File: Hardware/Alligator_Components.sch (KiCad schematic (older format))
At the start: 113 parts, among them J1 SWD_Header, J2 Eurorack_10_pin_power, J3 Conn_01x08_Female, J4 Conn_01x08_Female, J5 Conn_01x08_Female, J6 Conn_01x08_Female, SW1 SW_SPST, SW2 SW_SPDT_MSM, U1 STM32H743ZITx, U2 IS42S16400J-xC, U3 PCM5100APW, U4 SSI2164, U5 MCP6004, U6 MCP6004, U7 TL074, U8 LM1117-3.3, Y1 8MHz 20pF

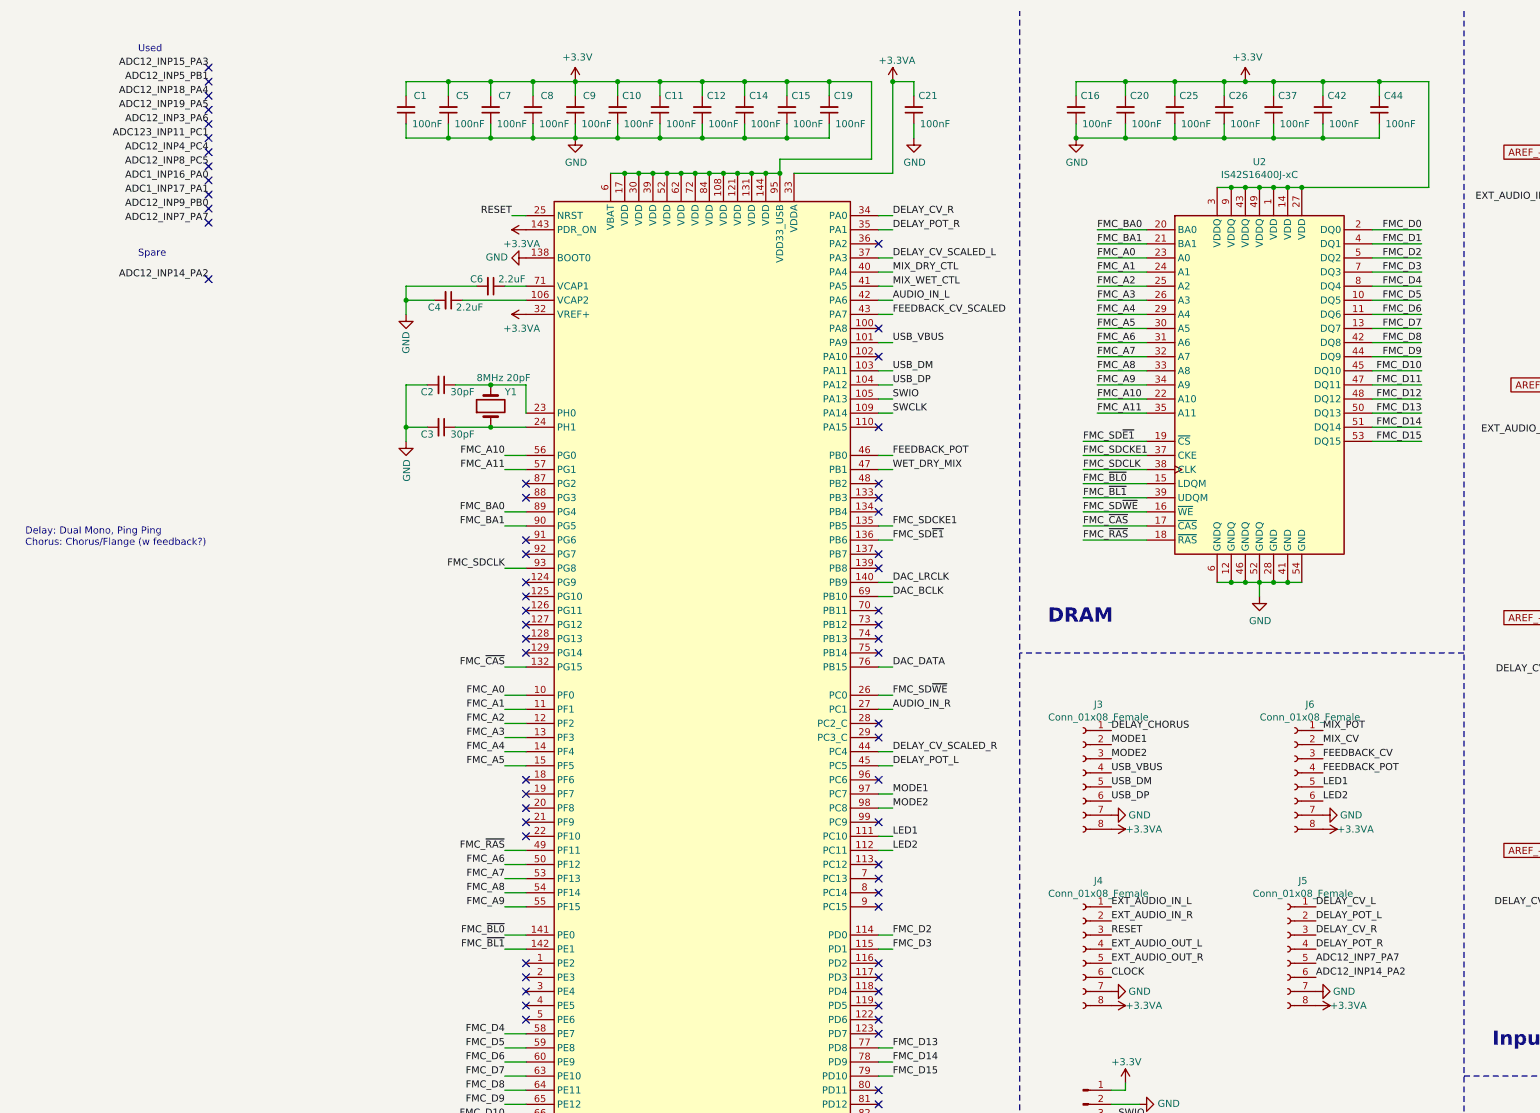
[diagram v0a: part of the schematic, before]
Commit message: Further routing of PCB
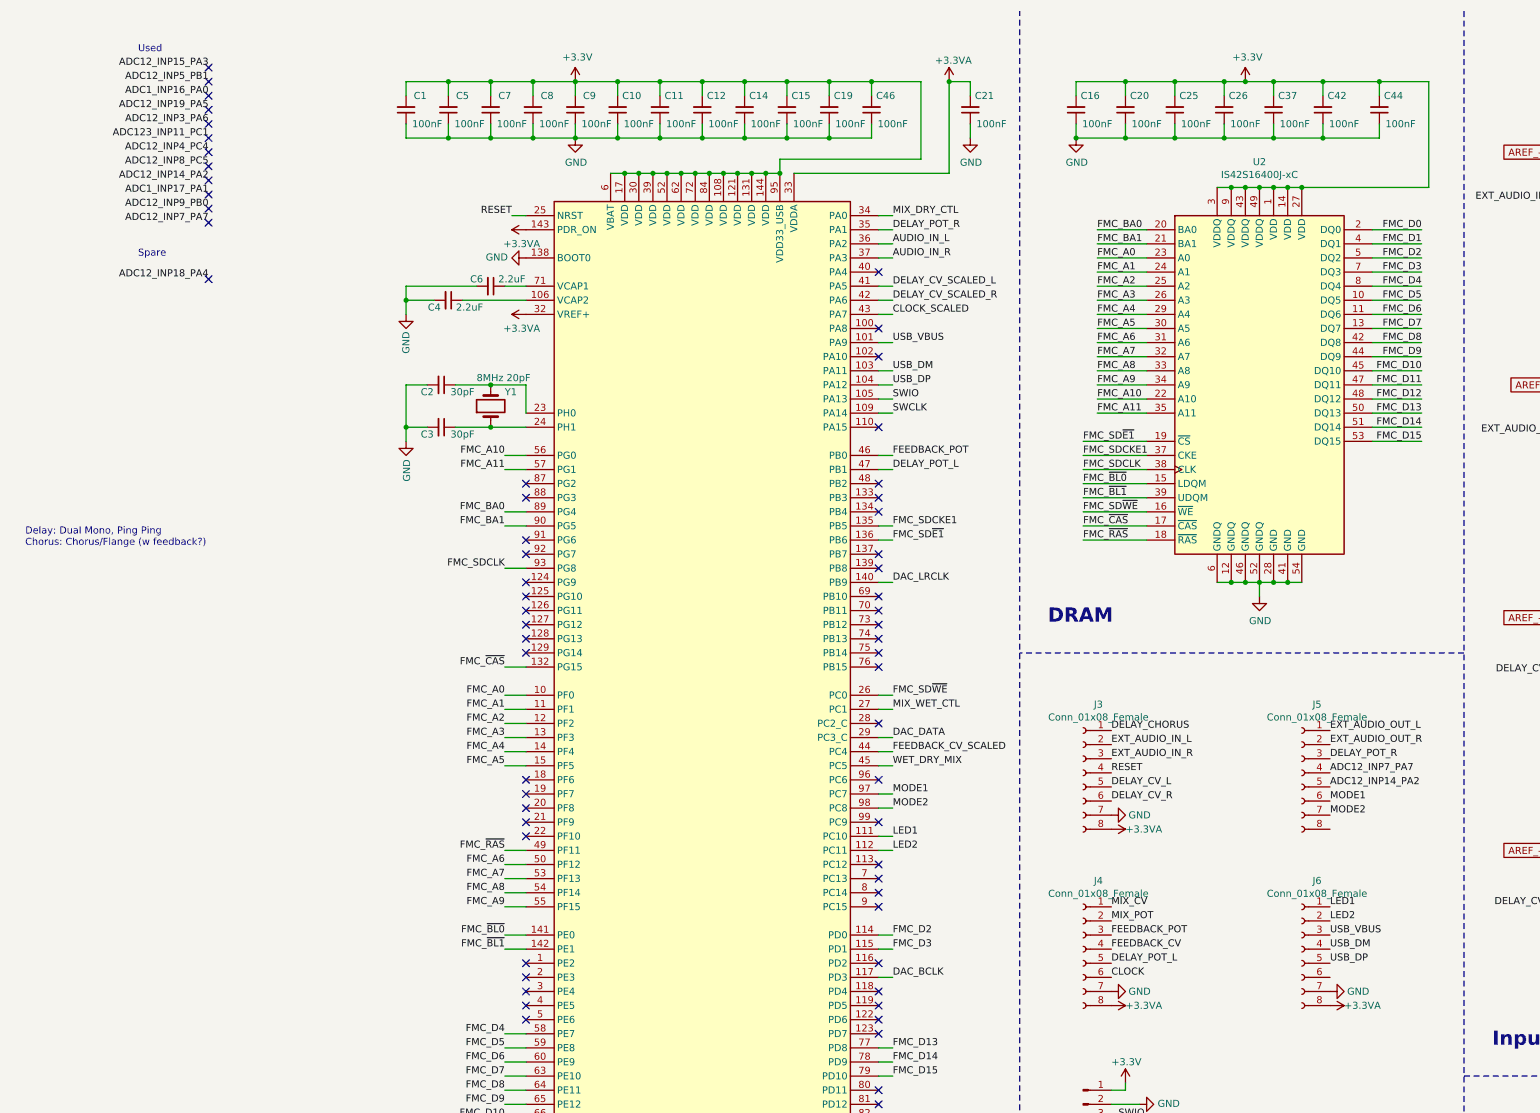
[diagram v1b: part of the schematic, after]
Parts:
- added C46: 100nF, Capacitors_SMD:C_0603_HandSoldering, symbol Device:C_Small
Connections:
- net +3.3VA: no longer J5.8 (Pin_8)
- net +3V3: now also C46.2
- net ADC12_INP14_PA2: now also J5.5 (Pin_5); no longer J5.6 (Pin_6)
- net ADC12_INP7_PA7: now also J5.4 (Pin_4); no longer J5.5 (Pin_5)
- net AUDIO_IN_L: now also U1.36 (PA2); no longer U1.42 (PA6)
- net AUDIO_IN_R: now also U1.37 (PA3); no longer U1.27 (PC1)
- net CLOCK_SCALED: now also U1.43 (PA7)
- net DAC_BCLK: now also U1.117 (PD3); no longer U1.69 (PB10)
- net DAC_DATA: now also U1.29 (PC3_C); no longer U1.76 (PB15)
- net DELAY_CV_L: now also J3.5 (Pin_5); no longer J5.1 (Pin_1)
- net DELAY_CV_R: now also J3.6 (Pin_6); no longer J5.3 (Pin_3), U1.34 (PA0)
- net DELAY_CV_SCALED_L: now also U1.41 (PA5); no longer U1.37 (PA3)
- net DELAY_CV_SCALED_R: now also U1.42 (PA6); no longer U1.44 (PC4)
- net DELAY_POT_L: now also J4.5 (Pin_5), U1.47 (PB1); no longer J5.2 (Pin_2), U1.45 (PC5)
- net DELAY_POT_R: now also J5.3 (Pin_3); no longer J5.4 (Pin_4)
- net EXT_AUDIO_IN_L: now also J3.2 (Pin_2); no longer J4.1 (Pin_1)
- net EXT_AUDIO_IN_R: now also J3.3 (Pin_3); no longer J4.2 (Pin_2)
- net EXT_AUDIO_OUT_L: now also J5.1 (Pin_1); no longer J4.4 (Pin_4)
- net EXT_AUDIO_OUT_R: now also J5.2 (Pin_2); no longer J4.5 (Pin_5)
- net FEEDBACK_CV: now also J4.4 (Pin_4); no longer J6.3 (Pin_3)
- net FEEDBACK_CV_SCALED: now also U1.44 (PC4); no longer U1.43 (PA7)
- net FEEDBACK_POT: now also J4.3 (Pin_3); no longer J6.4 (Pin_4)
- net GND: now also C46.1; no longer J5.7 (Pin_7)
- net LED1: now also J6.1 (Pin_1); no longer J6.5 (Pin_5)
- net LED2: now also J6.2 (Pin_2); no longer J6.6 (Pin_6)
- net MIX_CV: now also J4.1 (Pin_1); no longer J6.2 (Pin_2)
- net MIX_DRY_CTL: now also U1.34 (PA0); no longer U1.40 (PA4)
- net MIX_POT: now also J4.2 (Pin_2); no longer J6.1 (Pin_1)
- net MIX_WET_CTL: now also U1.27 (PC1); no longer U1.41 (PA5)
- net MODE1: now also J5.6 (Pin_6); no longer J3.2 (Pin_2)
- net MODE2: now also J5.7 (Pin_7); no longer J3.3 (Pin_3)
- net RESET: now also J3.4 (Pin_4); no longer J4.3 (Pin_3)
- net USB_DM: now also J6.4 (Pin_4); no longer J3.5 (Pin_5)
- net USB_DP: now also J6.5 (Pin_5); no longer J3.6 (Pin_6)
- net USB_VBUS: now also J6.3 (Pin_3); no longer J3.4 (Pin_4)
- net WET_DRY_MIX: now also U1.45 (PC5); no longer U1.47 (PB1)
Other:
- moved on the sheet: C21, J5, J6

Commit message: Continued routing and reorganising PCB
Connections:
- net +3.3VA: now also J5.2 (Pin_2)
- net +3V3: no longer U1.6 (VBAT)
- net ADC12_INP14_PA2: no longer J5.5 (Pin_5)
- net ADC12_INP7_PA7: no longer J5.4 (Pin_4)
- net DAC_OUT_AMP_L: now also R14.2; no longer R10.2
- net DAC_OUT_AMP_R: now also R10.2; no longer R14.2
- net DELAY_CHORUS: now also J6.6 (Pin_6), U1.119 (PD5); no longer J3.1 (Pin_1)
- net DELAY_POT_R: now also J5.6 (Pin_6); no longer J5.3 (Pin_3)
- net DRY_OUT_L: now also U4.5 (I_OUT2); no longer U4.4 (I_OUT1)
- net DRY_OUT_R: now also U4.4 (I_OUT1); no longer U4.5 (I_OUT2)
- net EXT_AUDIO_OUT_L: now also J5.5 (Pin_5); no longer J5.1 (Pin_1)
- net EXT_AUDIO_OUT_R: now also J5.4 (Pin_4); no longer J5.2 (Pin_2)
- net GND: now also J5.1 (Pin_1)
- net MODE1: now also J5.7 (Pin_7); no longer J5.6 (Pin_6)
- net MODE2: now also J5.8 (Pin_8); no longer J5.7 (Pin_7)
- net at C2.1, Y1.2: no longer U1.23 (PH0)
- no-connect marks 68 -> 67
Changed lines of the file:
@@
 	1500 3450 1750 3450
-Wire Wire Line
-	1750 3350 1750 3150
 Wire Wire Line
 	1750 3150 1500 3150
@@
 Text Label 4350 8050 0    50   ~ 0
 FMC_D15
-Wire Wire Line
-	2450 1650 2550 1650
 Wire Wire Line
 	2550 8850 2650 8850
@@
 Wire Wire Line
 	4350 3750 4250 3750
-Wire Wire Line
-	2350 1650 2450 1650
-Connection ~ 2450 1650
 NoConn ~ 1750 3850
 NoConn ~ 1750 3950
@@
 NoConn ~ 4250 7250
 NoConn ~ 4250 7450
-NoConn ~ 4250 7550
 NoConn ~ 4250 7650
 NoConn ~ 4250 7750
@@
 Text Label 5900 5700 0    50   ~ 0
 EXT_AUDIO_IN_L
-Text Label 7450 5700 0    50   ~ 0
+Text Label 7450 5900 0    50   ~ 0
 EXT_AUDIO_OUT_R
-Text Label 7450 5600 0    50   ~ 0
+Text Label 7450 6000 0    50   ~ 0
 EXT_AUDIO_OUT_L
 Text Label 16450 6800 0    50   ~ 0
@@
 Text Label 16450 5200 0    50   ~ 0
 EXT_AUDIO_OUT_L
+Text Label 15900 9150 0    50   ~ 0
+WET_OUT_L
 Text Label 15900 8850 0    50   ~ 0
-WET_OUT_L
-Text Label 15900 9150 0    50   ~ 0
 WET_OUT_R
 Text Label 15900 9450 0    50   ~ 0
@@
 	-1   0    0    1
 $EndComp
-Text Label 14050 8850 2    50   ~ 0
+Text Label 14050 9150 2    50   ~ 0
 DAC_OUT_AMP_L
 Wire Wire Line
@@
 Wire Wire Line
 	14750 9550 14750 9600
-Text Label 14050 9150 2    50   ~ 0
+Text Label 14050 8850 2    50   ~ 0
 DAC_OUT_AMP_R
 Wire Wire Line
@@
 Text Label 5900 7250 0    50   ~ 0
 DELAY_POT_L
-Text Label 7450 5800 0    50   ~ 0
+Text Label 7450 6100 0    50   ~ 0
 DELAY_POT_R
 Text Label 5900 7050 0    50   ~ 0
@@
 Wire Wire Line
 	14900 1750 14950 1750
-Text Label 5900 5600 0    50   ~ 0
+Text Label 7450 7350 0    50   ~ 0
 DELAY_CHORUS
 Text Notes -1800 4300 0    50   ~ 0
 Delay: Dual Mono, Ping Ping\nChorus: Chorus/Flange (w feedback?)
-Text Label 7450 6100 0    50   ~ 0
+Text Label 7450 6200 0    50   ~ 0
 MODE1
-Text Label 7450 6200 0    50   ~ 0
+Text Label 7450 6300 0    50   ~ 0
 MODE2
 $Comp
@@
 	0    1    1    0
 $EndComp
-Text Label 7450 6000 0    50   ~ 0
-ADC12_INP14_PA2
-Text Label 7450 5900 0    50   ~ 0
-ADC12_INP7_PA7
 $Comp
 L power:GNDA #PWR016
@@
 Wire Wire Line
 	4550 1000 4200 1000
-Connection ~ 3550 1650
 Connection ~ 3900 1000
 Wire Wire Line
@@
 Text Label 7450 6950 0    50   ~ 0
 LED2
+$Comp
+L power:GND #PWR0113
+U 1 1 60A8280D
+P 7450 5600
+F 0 "#PWR0113" H 7450 5350 50  0001 C CNN
+F 1 "GND" V 7450 5400 50  0000 C CNN
+F 2 "" H 7450 5600 50  0001 C CNN
+F 3 "" H 7450 5600 50  0001 C CNN
+	1    7450 5600
+	0    -1   -1   0
+$EndComp
+$Comp
+L power:+3.3VA #PWR0124
+U 1 1 60A82817
+P 7450 5700
+F 0 "#PWR0124" H 7450 5550 50  0001 C CNN
+F 1 "+3.3VA" V 7450 5800 50  0000 L CNN
+F 2 "" H 7450 5700 50  0001 C CNN
+F 3 "" H 7450 5700 50  0001 C CNN
+	1    7450 5700
+	0    1    1    0
+$EndComp
+Text Label 4350 7550 0    50   ~ 0
+DELAY_CHORUS
+Wire Wire Line
+	1750 3250 1750 3150
+Wire Wire Line
+	2450 1650 2550 1650
+Connection ~ 3550 1650
+Wire Wire Line
+	4250 7550 4350 7550
 $EndSCHEMATC

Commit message: Further updates to pcb layout
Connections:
- net +3V3: now also U1.6 (VBAT)
- net DELAY_CHORUS: now also J6.1 (Pin_1), U1.113 (PC12); no longer J6.6 (Pin_6), U1.119 (PD5)
- net DELAY_CV_SCALED_L: now also U1.34 (PA0); no longer U1.41 (PA5)
- net LED1: now also J6.3 (Pin_3); no longer J6.1 (Pin_1)
- net MIX_DRY_CTL: now also U1.40 (PA4); no longer U1.34 (PA0)
- net MIX_WET_CTL: now also U1.41 (PA5); no longer U1.27 (PC1)
- net MODE1: now also U1.1 (PE2); no longer U1.97 (PC7)
- net MODE2: now also U1.2 (PE3); no longer U1.98 (PC8)
- net USB_DM: now also J6.5 (Pin_5); no longer J6.4 (Pin_4)
- net USB_DP: now also J6.4 (Pin_4); no longer J6.5 (Pin_5)
- net USB_VBUS: now also J6.6 (Pin_6); no longer J6.3 (Pin_3)
- net at C2.1, Y1.2: now also U1.23 (PH0)
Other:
- moved on the sheet: J1, J3, J4, J5, J6

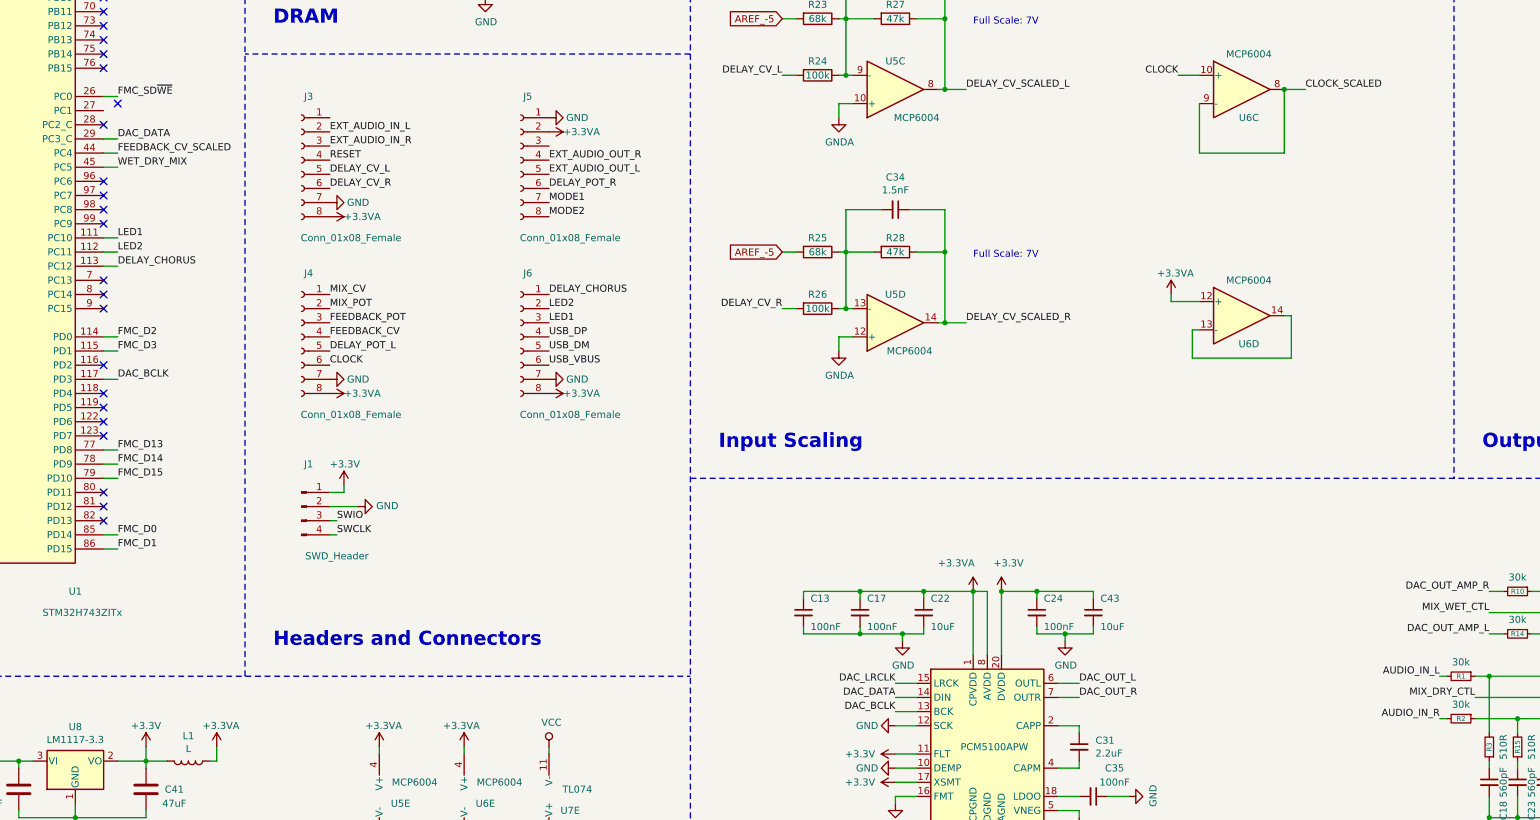
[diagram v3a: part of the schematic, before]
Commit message: Error pass of schematic and PCB - power rails still need routing
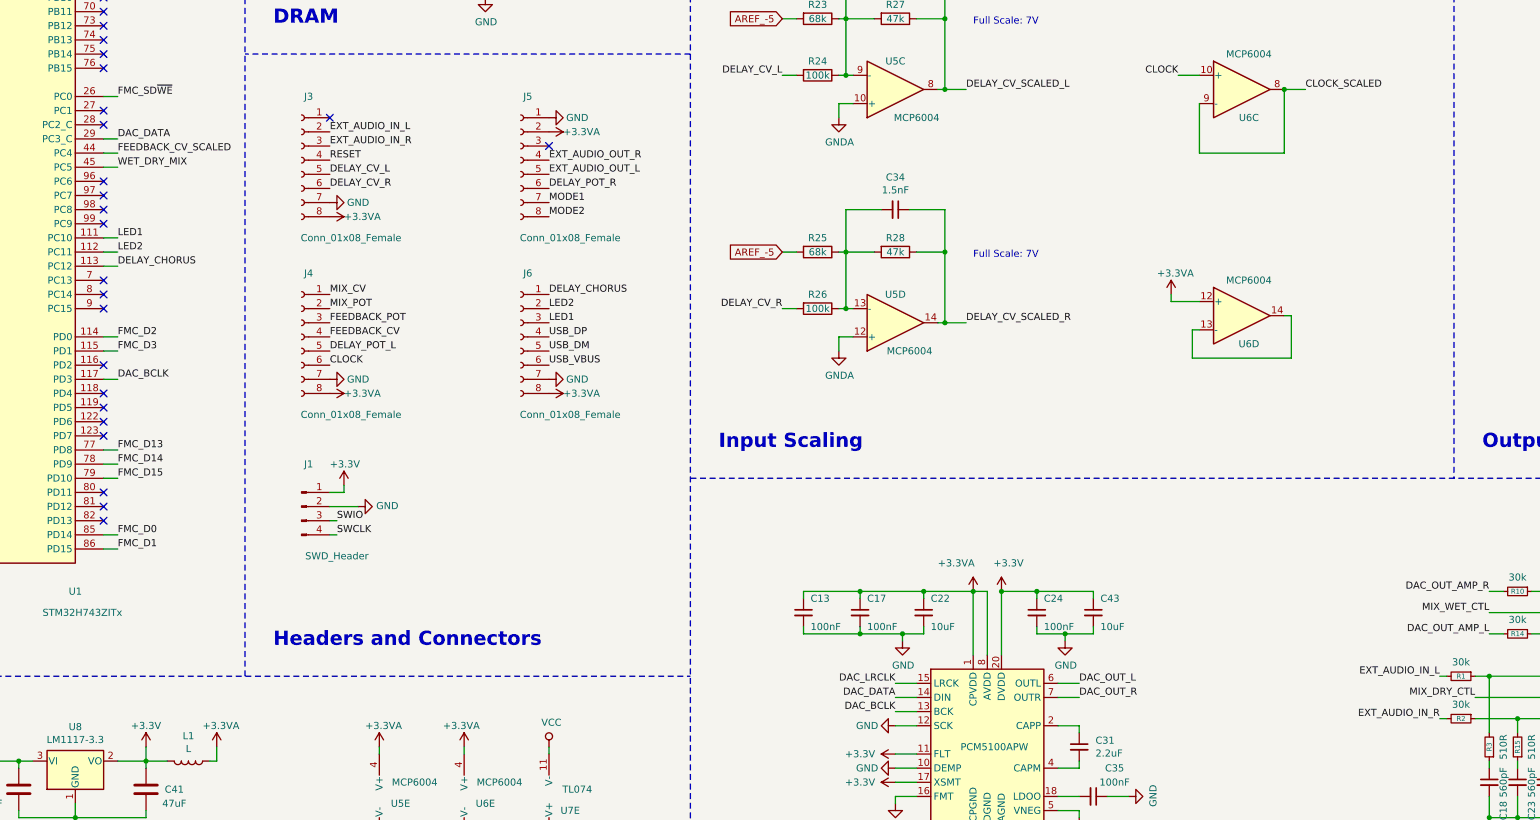
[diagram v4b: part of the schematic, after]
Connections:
- net AUDIO_IN_L: no longer R1.2
- net AUDIO_IN_R: no longer R2.2
- net EXT_AUDIO_IN_L: now also R1.2
- net EXT_AUDIO_IN_R: now also R2.2
- no-connect marks 67 -> 69
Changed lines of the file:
@@
 	13950 9450 14050 9450
 Text Label 13700 9750 2    50   ~ 0
-AUDIO_IN_R
+EXT_AUDIO_IN_R
 Text Label 13700 9450 2    50   ~ 0
-AUDIO_IN_L
+EXT_AUDIO_IN_L
 Text Label 13950 9600 2    50   ~ 0
 MIX_DRY_CTL
@@
 Wire Wire Line
 	4350 2150 4250 2150
-NoConn ~ 4350 5400
+NoConn ~ 4250 5450
 Text Label 7400 6950 0    50   ~ 0
 LED1
@@
 	2350 1650 2450 1650
 Connection ~ 2450 1650
+NoConn ~ 7400 5700
+NoConn ~ 5850 5500
 $EndSCHEMATC
